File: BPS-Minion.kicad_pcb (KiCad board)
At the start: 2 copper layers, 85 x 152 mm, 219 parts, among them J10 TopConn, J11 TopConn, J2 BMS1OTP, J3 BMS2OTP, J4 Conn_01x24_Female, J5 Conn_01x24_Female, J6 TopConn, J7 TopConn, J8 TopConn, J9 TopConn, U10 LM321, U11 ADS7953SBDBT, U12 MIC5317-2.5xM5, U2 BQ7695201PFBR, U3 ISO1640BDR, U4 EL3H7, U5 BQ7695201PFBR, U6 ISO1640BDR, U7 EL3H7, U8 LM321, U9 ADS7953SBDBT

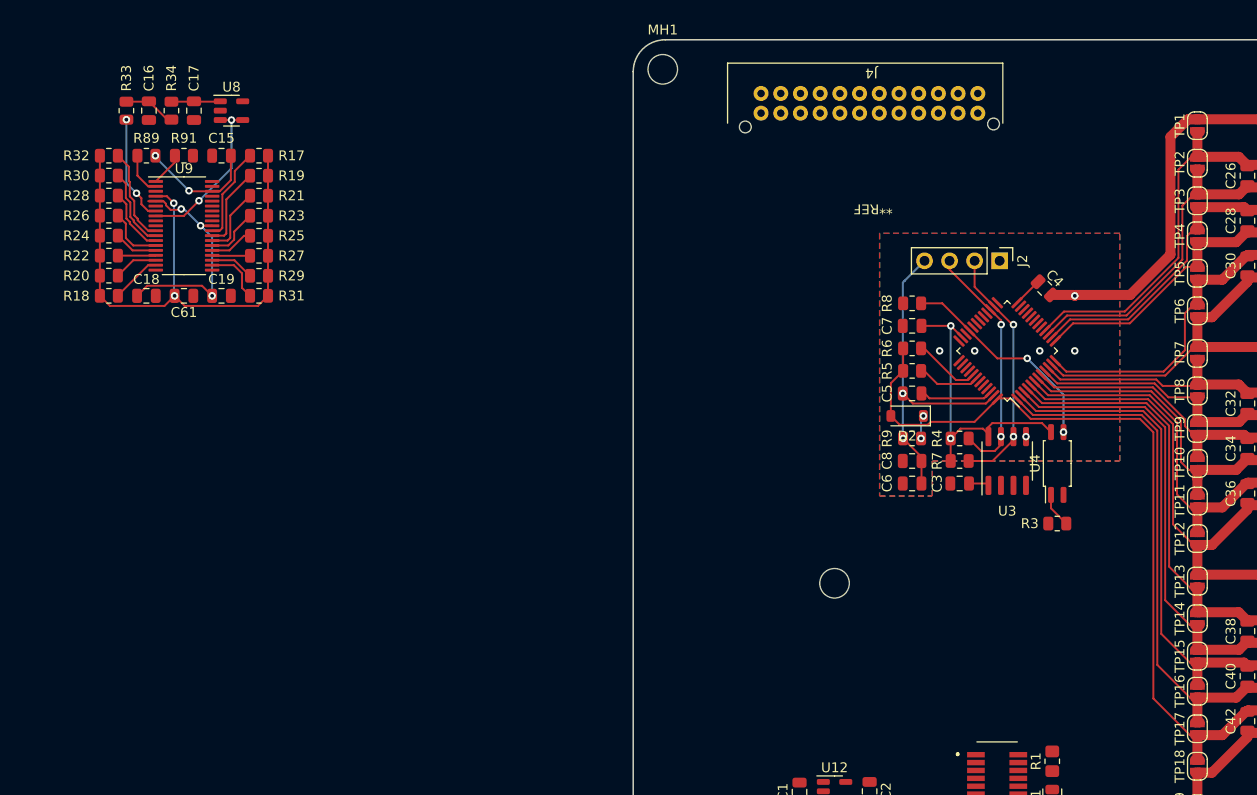
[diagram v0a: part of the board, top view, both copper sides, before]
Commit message: update solder mask
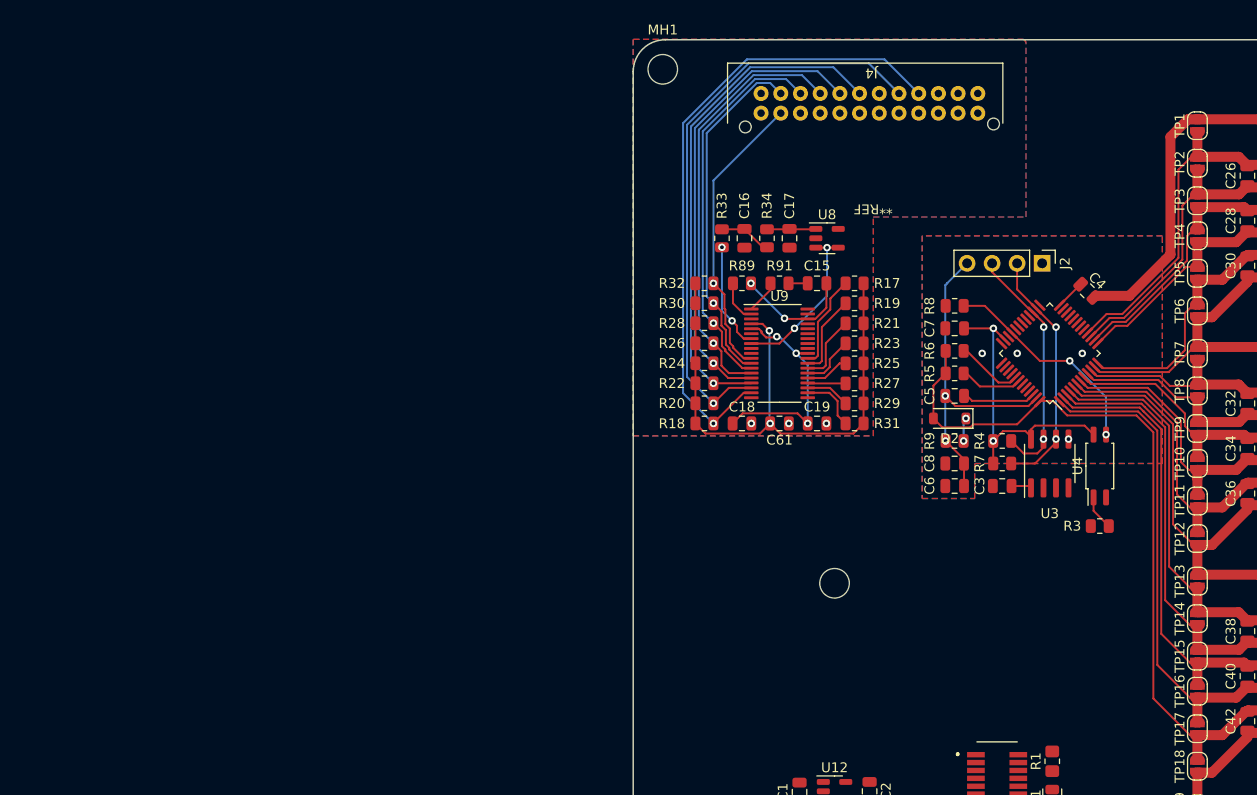
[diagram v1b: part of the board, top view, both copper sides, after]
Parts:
- moved R29 61.8 mm to (71.1, 63.8)
- moved R31 61.8 mm to (71.1, 65.8)
- moved C19 61.8 mm to (67.3, 65.8)
- moved R17 61.8 mm to (71.1, 51.6)
- moved R18 61.8 mm to (55.9, 65.8)
- moved R19 61.8 mm to (71.1, 53.6)
- moved R34 61.8 mm to (62.2, 47.0)
- moved R20 61.8 mm to (55.9, 63.7)
- moved R22 61.8 mm to (55.9, 61.7)
- moved R24 61.8 mm to (55.9, 59.7)
- moved R26 61.8 mm to (55.9, 57.6)
- moved R28 61.8 mm to (55.9, 55.6)
- moved R30 61.8 mm to (55.9, 53.6)
- moved R32 61.8 mm to (55.9, 51.6)
- moved C15 61.8 mm to (67.3, 51.6)
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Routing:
- net /Temperature/temp9: track 5.16 -> 64.9 mm, vias 0 -> 1
- net /Temperature/temp10: track 4.49 -> 59.2 mm, vias 0 -> 1
- net /Temperature/temp11: track 3.86 -> 51.6 mm, vias 0 -> 1
- net /Temperature/temp12: track 4.47 -> 47.2 mm, vias 0 -> 1
- net /Temperature/temp13: track 5.96 -> 43.6 mm, vias 0 -> 1
- net /Temperature/temp14: track 6.68 -> 39.3 mm, vias 0 -> 1
- net /Temperature/temp15: track 8.18 -> 35.8 mm, vias 0 -> 1
- net /Temperature/temp16: track 9.66 -> 29.8 mm, vias 0 -> 1
- net /BMS/cell5: track 42.3 -> 37.6 mm
- net /BMS/cell4: track 34.5 -> 29.8 mm
- net /BMS/cell13: track 51.6 -> 47.2 mm
- net /BMS/cell7: track 30.5 -> 26.1 mm
- net /BMS/cell10: track 40.7 -> 36.3 mm
- net /BMS/cell9: track 36.6 -> 32.1 mm
- net /BMS/cell15: track 58.9 -> 54.4 mm
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- added copper zone on B.Cu, net GNDA
- added copper zone on F.Cu, net GNDA
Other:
- rule pad_to_mask_clearance: 0.2 -> 0.038
- rule solder_mask_min_width: 0.25 -> 0.1

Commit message: literal piss and shit
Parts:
- C11, C5: value .47u -> 0.47u
- R1, R13: footprint Resistor_SMD:R_0805_2012Metric_Pad1.20x1.40mm_HandSolder -> Resistor_SMD:R_0805_2012Metric
- R35, R36, R37, R38, R39, R40, R41, R42, R43, R44, R45, R46, R47, R48, R49, R50: moved to F.Cu
- moved MH3 162.2 mm to (90.5, 18.4)
- moved J11 161.7 mm to (3.85, 44.9), turned to 0 degrees
- moved MH4 155.2 mm to (90.5, 25.9)
- moved R83 151.4 mm to (10.5, 48.4), turned to 0 degrees
- moved C55 151.3 mm to (6.08, 48.4), turned to 0 degrees
- moved R84 150.9 mm to (10.5, 51.4), turned to 0 degrees
- moved R85 150.5 mm to (10.5, 54.3), turned to 0 degrees
- moved C57 150.3 mm to (6.08, 54.5), turned to 0 degrees
- moved R86 150.0 mm to (10.5, 57.3), turned to 0 degrees
- moved R87 149.6 mm to (10.5, 60.2), turned to 0 degrees
- moved C59 149.3 mm to (6.08, 60.5), turned to 0 degrees
- moved R88 149.1 mm to (10.5, 63.2), turned to 0 degrees
- moved C56 148.3 mm to (6.08, 51.5), turned to 0 degrees
- moved R16 147.8 mm to (21.9, 6.88)
- moved C58 147.2 mm to (6.08, 57.5), turned to 0 degrees
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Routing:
- net GND2: track 80.1 -> 0.00 mm
- net /Temperature1/temp1: track 68.3 -> 0.00 mm, vias 3 -> 0
- net /Temperature/temp9: track 64.9 -> 0.00 mm, vias 1 -> 0
- net /Temperature1/temp2: track 62.5 -> 0.00 mm, vias 3 -> 0
- net /Temperature/temp10: track 59.2 -> 0.00 mm, vias 1 -> 0
- net +2V5: track 58.8 -> 0.00 mm, vias 2 -> 0
- net /Temperature1/temp8: track 55.2 -> 0.00 mm, vias 3 -> 0
- net /BMS/cell15: track 54.4 -> 0.00 mm
- net /Temperature/temp11: track 51.6 -> 0.00 mm, vias 1 -> 0
- net /BMS/cell11: track 51.0 -> 0.00 mm
- net /Temperature1/temp7: track 50.6 -> 0.00 mm, vias 3 -> 0
- net /BMS/cell14: track 50.5 -> 0.00 mm
- net /BMS/cell13: track 47.2 -> 0.00 mm
- net /Temperature/temp12: track 47.2 -> 0.00 mm, vias 1 -> 0
- net /Temperature/temp13: track 43.6 -> 0.00 mm, vias 1 -> 0
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- removed copper zone on B.Cu, net GND1
- removed copper zone on F.Cu, net GND1
- removed copper zone on B.Cu, net GNDA
- removed copper zone on F.Cu, net GNDA
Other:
- board outline removed
- board text removed: "Grid size is .2540 mm"

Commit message: a
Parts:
- C25, C26, C27, C28, C29, C30, C31, C32, C33, C34, C35, C36, C37, C38, C39, C40, C41, C42, C43, C44, C45, C46, C47, C48, C49, C50, C51, C52, C53, C54, C55, C56, C57, C58, C59, C60, R53, R54, R55, R56, R57, R58, R59, R60, R61, R62, R63, R64, R65, R66, R67, R68, R69, R70, R71, R72, R73, R74, R75, R76, R77, R78, R79, R80, R81, R82, R83, R84, R85, R86, R87, R88, TP1, TP10, TP11, TP12, TP13, TP14, TP15, TP16, TP17, TP18, TP19, TP2, TP20, TP21, TP22, TP23, TP24, TP25, TP26, TP27, TP28, TP29, TP3, TP30, TP31, TP32, TP33, TP34, TP35, TP36, TP4, TP5, TP6, TP7, TP8, TP9: moved to B.Cu
- moved R21 251.9 mm to (253.0, -37.0), turned to 90 degrees
- moved R25 250.1 mm to (257.0, -37.0), turned to 90 degrees
- moved R20 246.9 mm to (249.0, -37.0), turned to 90 degrees
- moved R18 246.0 mm to (251.0, -37.0), turned to 90 degrees
- moved R23 245.6 mm to (255.0, -37.0), turned to 90 degrees
- moved R19 239.9 mm to (251.0, -20.0), turned to -90 degrees
- moved R26 237.6 mm to (241.0, -37.0), turned to 90 degrees
- moved R24 236.4 mm to (243.0, -37.0), turned to 90 degrees
- moved R31 236.2 mm to (253.0, -20.0), turned to -90 degrees
- moved R17 235.7 mm to (249.0, -20.0), turned to -90 degrees
- moved R29 235.5 mm to (255.0, -20.0), turned to -90 degrees
- moved R22 235.4 mm to (245.0, -37.0), turned to 90 degrees
- moved R27 235.0 mm to (257.0, -20.0), turned to -90 degrees
- moved R30 228.8 mm to (237.0, -37.0), turned to 90 degrees
- moved R28 227.6 mm to (239.0, -37.0), turned to 90 degrees
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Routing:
- net /BMS/cell17: track 0.00 -> 13.9 mm
- net /BMS/cell5: track 0.00 -> 13.9 mm
- net /BMS/cell29: track 0.00 -> 13.9 mm
- net /BMS/cell23: track 0.00 -> 13.9 mm
- net /BMS/cell11: track 0.00 -> 13.9 mm
- net GND2: track 0.00 -> 12.8 mm
- net /BMS/cell15: track 0.00 -> 12.4 mm
- net /BMS/cell14: track 0.00 -> 12.0 mm
- net /BMS/cell12: track 0.00 -> 12.0 mm
- net /BMS/cell4: track 0.00 -> 11.8 mm
- net /BMS/cell10: track 0.00 -> 11.8 mm
- net /BMS/cell28: track 0.00 -> 11.8 mm
- net /BMS/cell22: track 0.00 -> 11.8 mm
- net /BMS/BatteryConnector6/cell5+: track 0.00 -> 11.8 mm
- net /BMS/cell13: track 0.00 -> 11.5 mm
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
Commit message: footprint changes
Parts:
- C1: value 10u -> 10uF
- C10, C13, C14, C15, C18, C19, C2, C20, C23, C24, C3, C7, C8: value 1u -> 1uF
- C11, C5: value 0.47u -> 0.47uF
- C12, C6: value 100p -> 100pF
- C16, C17, C21, C22: value 47n -> 47nF
- C4, C9: value 4.7u -> 4.7uF
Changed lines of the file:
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@@
         (effects (font (size 1 1) (thickness 0.15)))
     )
-    (fp_text value "47n" (at 0 1.68) (layer "F.Fab")
+    (fp_text value "47nF" (at 0 1.68) (layer "F.Fab")
         (effects (font (size 1 1) (thickness 0.15)))
     )
@@
         (effects (font (size 1 1) (thickness 0.15)))
     )
-    (fp_text value "1u" (at 0 1.68) (layer "F.Fab")
+    (fp_text value "1uF" (at 0 1.68) (layer "F.Fab")
         (effects (font (size 1 1) (thickness 0.15)))
     )
@@
         (effects (font (size 1 1) (thickness 0.15)))
     )
-    (fp_text value "1u" (at 0 1.68) (layer "F.Fab")
+    (fp_text value "1uF" (at 0 1.68) (layer "F.Fab")
         (effects (font (size 1 1) (thickness 0.15)))
     )
@@
         (effects (font (size 1 1) (thickness 0.15)))
     )
-    (fp_text value "1u" (at 0 1.68) (layer "F.Fab")
+    (fp_text value "1uF" (at 0 1.68) (layer "F.Fab")
         (effects (font (size 1 1) (thickness 0.15)))
     )
@@
         (effects (font (size 1 1) (thickness 0.15)))
     )
-    (fp_text value "1u" (at 0 1.68) (layer "F.Fab")
+    (fp_text value "1uF" (at 0 1.68) (layer "F.Fab")
         (effects (font (size 1 1) (thickness 0.15)))
     )
@@
         (effects (font (size 1 1) (thickness 0.15)))
     )
-    (fp_text value "47n" (at 0 1.68) (layer "F.Fab")
+    (fp_text value "47nF" (at 0 1.68) (layer "F.Fab")
         (effects (font (size 1 1) (thickness 0.15)))
     )
@@
         (effects (font (size 1 1) (thickness 0.15)))
     )
-    (fp_text value "4.7u" (at 0 1.68) (layer "F.Fab")
+    (fp_text value "4.7uF" (at 0 1.68) (layer "F.Fab")
         (effects (font (size 1 1) (thickness 0.15)))
     )
@@
         (effects (font (size 1 1) (thickness 0.15)))
     )
-    (fp_text value "4.7u" (at 0 1.68) (layer "F.Fab")
+    (fp_text value "4.7uF" (at 0 1.68) (layer "F.Fab")
         (effects (font (size 1 1) (thickness 0.15)))
     )
@@
         (effects (font (size 1 1) (thickness 0.15)))
     )
-    (fp_text value "47n" (at 0 1.68) (layer "F.Fab")
+    (fp_text value "47nF" (at 0 1.68) (layer "F.Fab")
         (effects (font (size 1 1) (thickness 0.15)))
     )
@@
         (effects (font (size 1 1) (thickness 0.15)))
     )
-    (fp_text value "1u" (at 0 1.68) (layer "F.Fab")
+    (fp_text value "1uF" (at 0 1.68) (layer "F.Fab")
         (effects (font (size 1 1) (thickness 0.15)))
     )
@@
         (effects (font (size 1 1) (thickness 0.15)))
     )
-    (fp_text value "1u" (at 0 1.68) (layer "F.Fab")
+    (fp_text value "1uF" (at 0 1.68) (layer "F.Fab")
         (effects (font (size 1 1) (thickness 0.15)))
     )
@@
         (effects (font (size 1 1) (thickness 0.15)))
     )
-    (fp_text value "1u" (at 0 1.68) (layer "F.Fab")
+    (fp_text value "1uF" (at 0 1.68) (layer "F.Fab")
         (effects (font (size 1 1) (thickness 0.15)))
     )
@@
         (effects (font (size 1 1) (thickness 0.15)))
     )
-    (fp_text value "100p" (at 0 1.68) (layer "F.Fab")
+    (fp_text value "100pF" (at 0 1.68) (layer "F.Fab")
         (effects (font (size 1 1) (thickness 0.15)))
     )
@@
         (effects (font (size 1 1) (thickness 0.15)))
     )
-    (fp_text value "0.47u" (at 0 1.68) (layer "F.Fab")
+    (fp_text value "0.47uF" (at 0 1.68) (layer "F.Fab")
         (effects (font (size 1 1) (thickness 0.15)))
     )
@@
         (effects (font (size 1 1) (thickness 0.15)))
     )
-    (fp_text value "1u" (at 0 1.68) (layer "F.Fab")
+    (fp_text value "1uF" (at 0 1.68) (layer "F.Fab")
         (effects (font (size 1 1) (thickness 0.15)))
     )
@@
         (effects (font (size 1 1) (thickness 0.15)))
     )
-    (fp_text value "47n" (at 0 1.68) (layer "F.Fab")
+    (fp_text value "47nF" (at 0 1.68) (layer "F.Fab")
         (effects (font (size 1 1) (thickness 0.15)))
     )
@@
         (effects (font (size 1 1) (thickness 0.15)))
     )
-    (fp_text value "1u" (at 0 1.68) (layer "F.Fab")
+    (fp_text value "1uF" (at 0 1.68) (layer "F.Fab")
         (effects (font (size 1 1) (thickness 0.15)))
     )
@@
         (effects (font (size 1 1) (thickness 0.15)))
     )
-    (fp_text value "10u" (at 0 1.68) (layer "F.Fab")
+    (fp_text value "10uF" (at 0 1.68) (layer "F.Fab")
         (effects (font (size 1 1) (thickness 0.15)))
     )
@@
         (effects (font (size 1 1) (thickness 0.15)))
     )
-    (fp_text value "0.47u" (at 0 1.68) (layer "F.Fab")
+    (fp_text value "0.47uF" (at 0 1.68) (layer "F.Fab")
         (effects (font (size 1 1) (thickness 0.15)))
     )
@@
         (effects (font (size 1 1) (thickness 0.15)))
     )
-    (fp_text value "1u" (at 0 1.68) (layer "F.Fab")
+    (fp_text value "1uF" (at 0 1.68) (layer "F.Fab")
         (effects (font (size 1 1) (thickness 0.15)))
     )
@@
         (effects (font (size 1 1) (thickness 0.15)))
     )
-    (fp_text value "1u" (at 0 1.68) (layer "F.Fab")
+    (fp_text value "1uF" (at 0 1.68) (layer "F.Fab")
         (effects (font (size 1 1) (thickness 0.15)))
     )
@@
         (effects (font (size 1 1) (thickness 0.15)))
     )
-    (fp_text value "1u" (at 0 1.68) (layer "F.Fab")
+    (fp_text value "1uF" (at 0 1.68) (layer "F.Fab")
         (effects (font (size 1 1) (thickness 0.15)))
     )
@@
         (effects (font (size 1 1) (thickness 0.15)))
     )
-    (fp_text value "1u" (at 0 1.68) (layer "F.Fab")
+    (fp_text value "1uF" (at 0 1.68) (layer "F.Fab")
         (effects (font (size 1 1) (thickness 0.15)))
     )
@@
         (effects (font (size 1 1) (thickness 0.15)))
     )
-    (fp_text value "100p" (at 0 1.68) (layer "F.Fab")
+    (fp_text value "100pF" (at 0 1.68) (layer "F.Fab")
         (effects (font (size 1 1) (thickness 0.15)))
     )

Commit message: drcs
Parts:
- J4, J5: footprint UTSVT_Connectors:PADP-24V-1-S -> UTSVT_Connectors:B24B-PADSS-F
- moved J4 22.0 mm to (235.0, -29.0)
- moved R18 16.0 mm to (250.0, -21.0), turned to -90 degrees
- moved R20 16.0 mm to (248.0, -21.0), turned to -90 degrees
- moved R21 16.0 mm to (252.0, -21.0), turned to -90 degrees
- moved R22 16.0 mm to (244.0, -21.0), turned to -90 degrees
- moved R23 16.0 mm to (254.0, -21.0), turned to -90 degrees
- moved R24 16.0 mm to (242.0, -21.0), turned to -90 degrees
- moved R25 16.0 mm to (256.0, -21.0), turned to -90 degrees
- moved R26 16.0 mm to (240.0, -21.0), turned to -90 degrees
- moved R28 16.0 mm to (238.0, -21.0), turned to -90 degrees
- moved R30 16.0 mm to (236.0, -21.0), turned to -90 degrees
- moved R17 3.00 mm to (249.0, -17.0)
- moved R19 3.00 mm to (251.0, -17.0)
- moved R27 3.00 mm to (257.0, -17.0)
- moved R29 3.00 mm to (255.0, -17.0)
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
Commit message: a
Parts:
- R17, R18, R19, R20, R21, R22, R23, R24, R25, R26, R27, R28, R29, R30, R31, R32, R35, R36, R37, R38, R39, R40, R41, R42, R43, R44, R45, R46, R47, R48, R49, R50: moved to B.Cu
- moved R40 361.5 mm to (242.0, 176.5), turned to -90 degrees
- moved R46 360.5 mm to (248.0, 176.5), turned to -90 degrees
- moved R42 358.6 mm to (244.0, 176.5), turned to -90 degrees
- moved R36 358.3 mm to (236.0, 176.5), turned to -90 degrees
- moved R48 357.7 mm to (250.0, 176.5), turned to -90 degrees
- moved R44 355.9 mm to (246.0, 176.5), turned to -90 degrees
- moved R38 355.4 mm to (238.0, 176.5), turned to -90 degrees
- moved R35 354.6 mm to (238.0, 166.5), turned to 90 degrees
- moved R50 353.7 mm to (250.0, 166.5), turned to 90 degrees
- moved R41 352.5 mm to (232.0, 176.5), turned to -90 degrees
- moved R39 350.5 mm to (234.0, 176.5), turned to -90 degrees
- moved R37 349.0 mm to (236.0, 166.5), turned to 90 degrees
- moved R43 346.9 mm to (230.0, 176.5), turned to -90 degrees
- moved R45 343.0 mm to (230.0, 166.5), turned to 90 degrees
- moved R47 340.1 mm to (232.0, 166.5), turned to 90 degrees
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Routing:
- net /BMS/cell1: track 10.5 -> 39.4 mm, vias 0 -> 1
- net /BMS/cell0: track 11.0 -> 39.2 mm, vias 0 -> 1
- net /BMS/cell18: track 11.0 -> 37.9 mm, vias 0 -> 1
- net /BMS/cell2: track 11.0 -> 35.6 mm, vias 0 -> 1
- net /BMS/cell32: track 11.0 -> 34.6 mm, vias 0 -> 1
- net /BMS/cell17: track 13.9 -> 37.4 mm, vias 0 -> 1
- net /BMS/cell19: track 10.5 -> 32.9 mm, vias 0 -> 1
- net /BMS/cell31: track 10.5 -> 32.1 mm, vias 0 -> 1
- net /BMS/cell15: track 12.4 -> 33.9 mm, vias 0 -> 1
- net /BMS/cell30: track 11.0 -> 31.8 mm, vias 0 -> 1
- net /BMS/cell3: track 11.4 -> 31.8 mm, vias 0 -> 1
- net /BMS/cell14: track 12.0 -> 30.2 mm, vias 0 -> 1
- net /BMS/cell4: track 11.8 -> 29.6 mm, vias 0 -> 1
- net /BMS/cell20: track 11.0 -> 28.1 mm, vias 0 -> 1
- net /BMS/cell13: track 11.5 -> 26.4 mm, vias 0 -> 1
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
